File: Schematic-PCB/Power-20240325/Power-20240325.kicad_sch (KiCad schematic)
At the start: 41 parts, among them J1 Conn_01x02_Pin, J2 Conn_01x05_Pin, J3 Conn_01x02_Pin, J4 Conn_01x02_Pin, J5 Conn_01x02_Pin, J6 Conn_01x02_Pin, Q1 PMOS, Q2 NMOS, SW1 SW_SPDT, SW2 Locker-SW, SW3 SW_SPDT, U1 PIC12F683-IMC

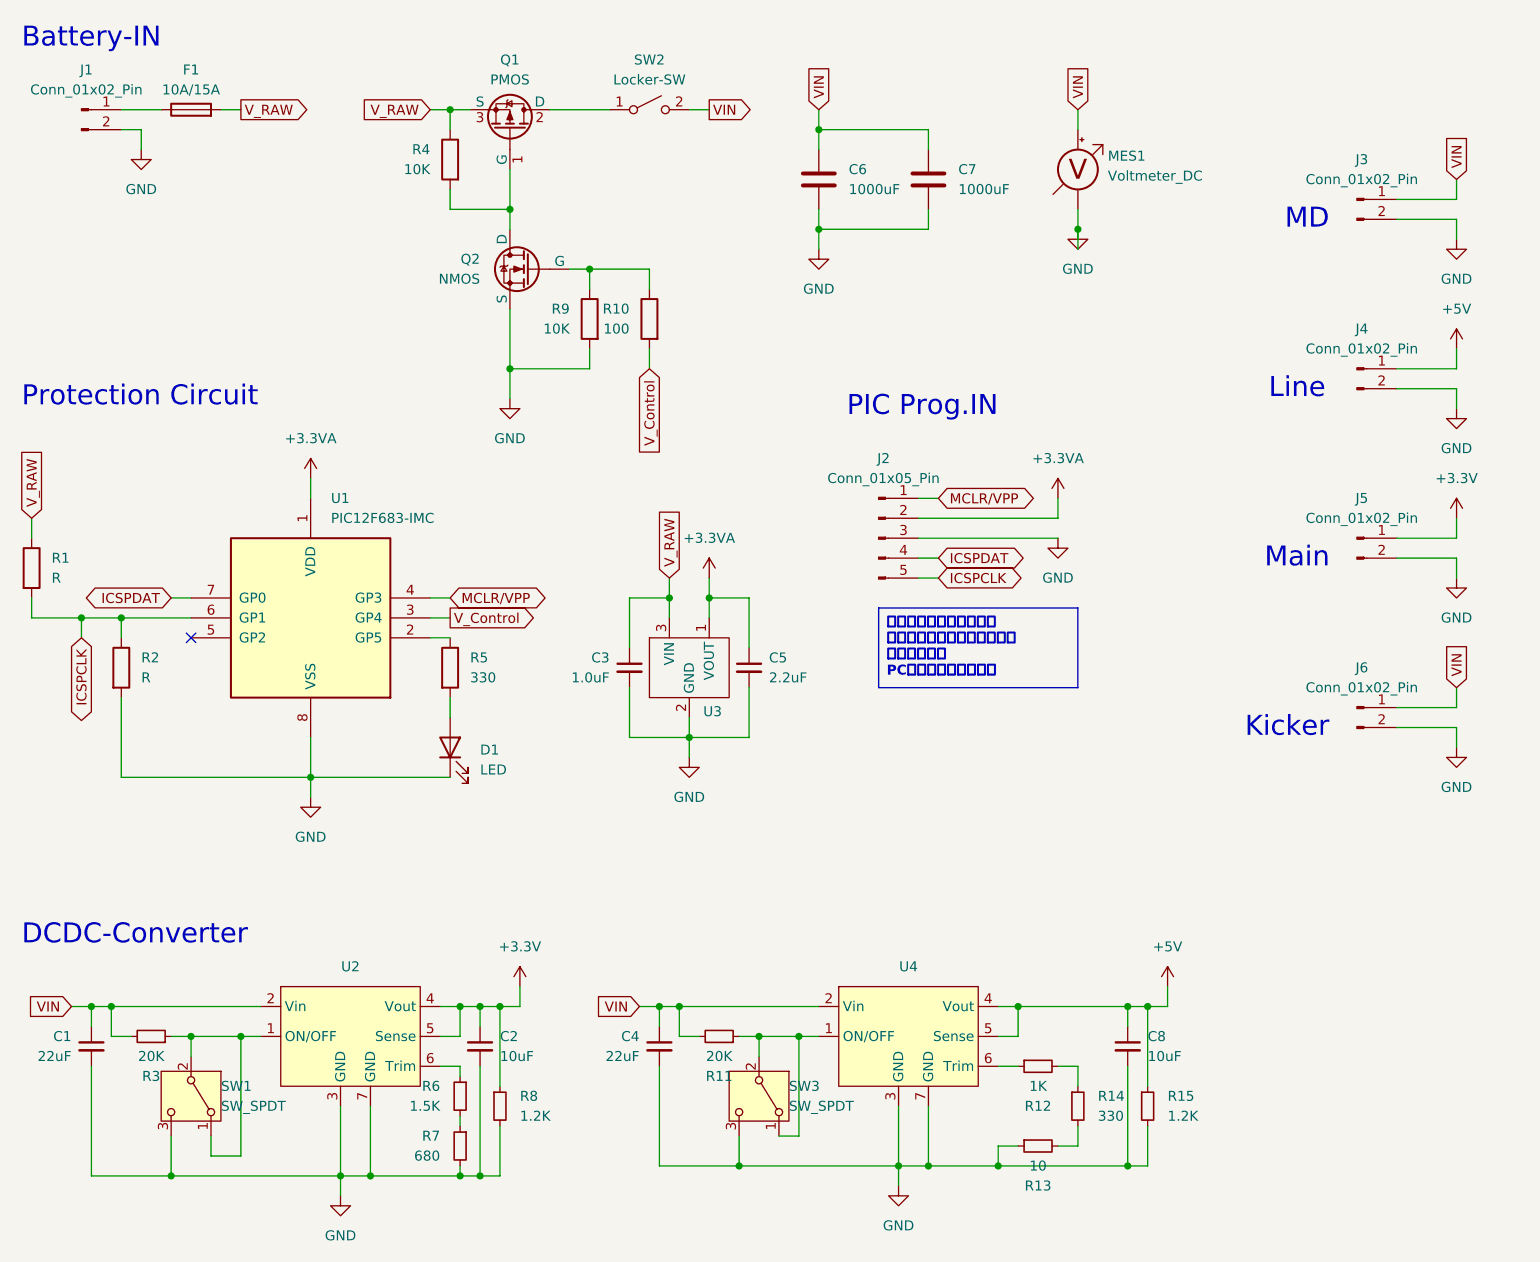
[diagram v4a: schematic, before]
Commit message: 電源基板PCB仮完成
DRをお願いします。
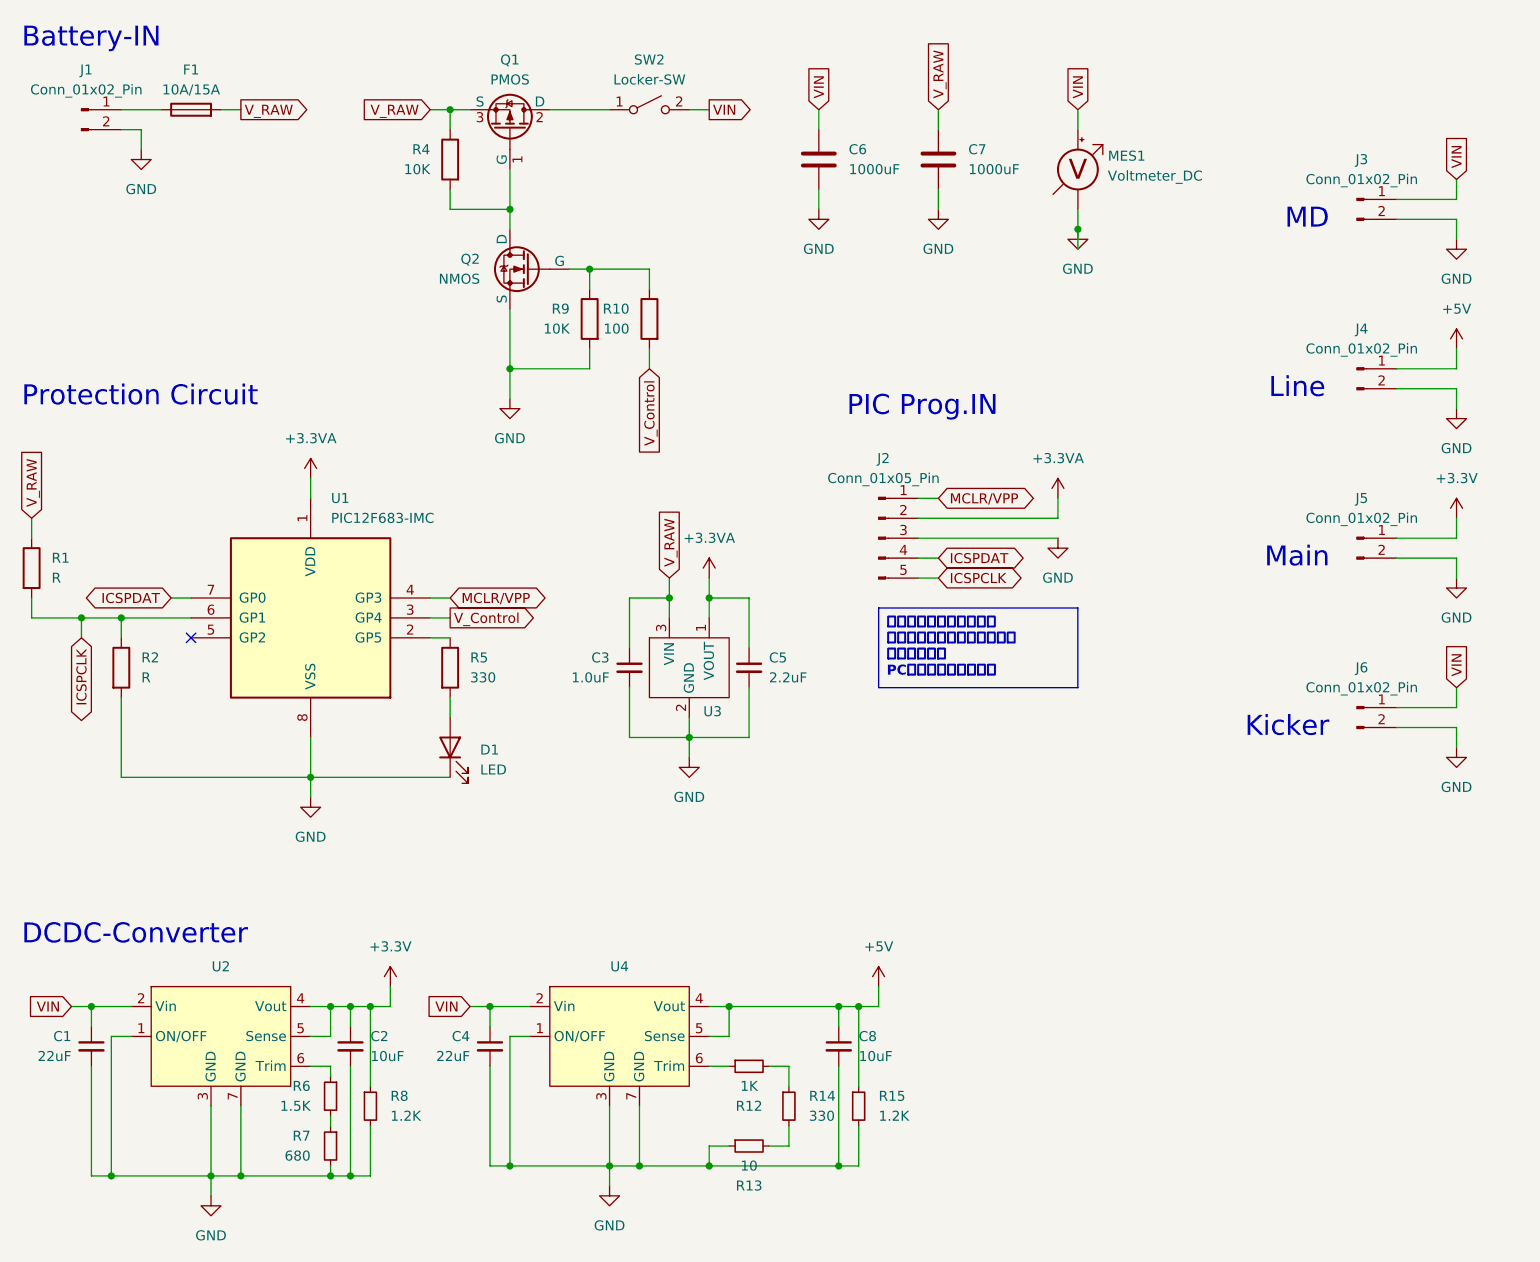
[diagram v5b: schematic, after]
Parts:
- removed R11, R3: 20K, Resistor_SMD:R_0603_1608Metric, symbol Device:R_Small
- removed SW1, SW3: SW_SPDT, @2024-Power:SS12D01G4, symbol Switch:SW_SPDT
- D1: footprint LED_SMD:LED_0805_2012Metric -> LED_THT:LED_D3.0mm
- J3: footprint (none) -> @2024-Power:XT30PW-M
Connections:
- net GND: now also U2.1 (ON/OFF), U4.1 (ON/OFF)
- net VIN: no longer C7.1
- net V_RAW: now also C7.1
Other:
- moved on the sheet: C2, C4, C6, C7, C8, R12, R13, R14, R15, R6, R7, R8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

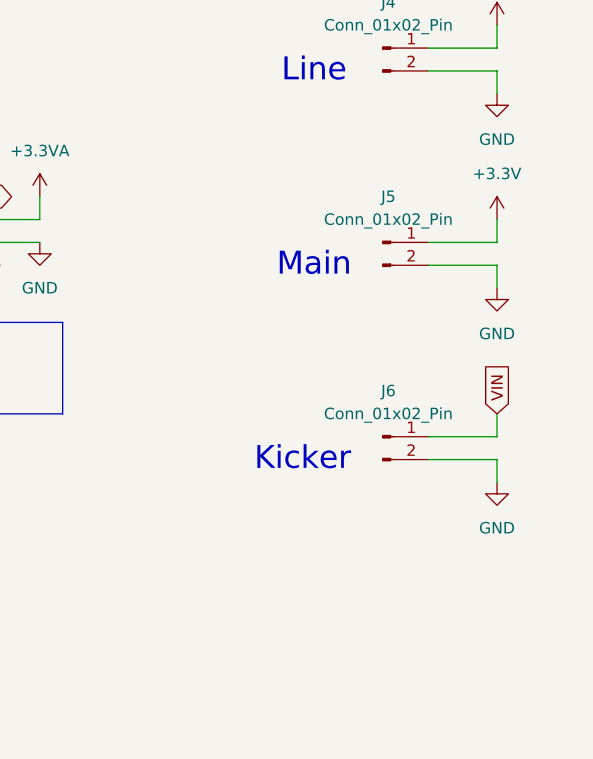
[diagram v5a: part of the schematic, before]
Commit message: 電源基板の回路図/PCBデザインを更新しました。
メイン基板への供給ラインを増やしました。
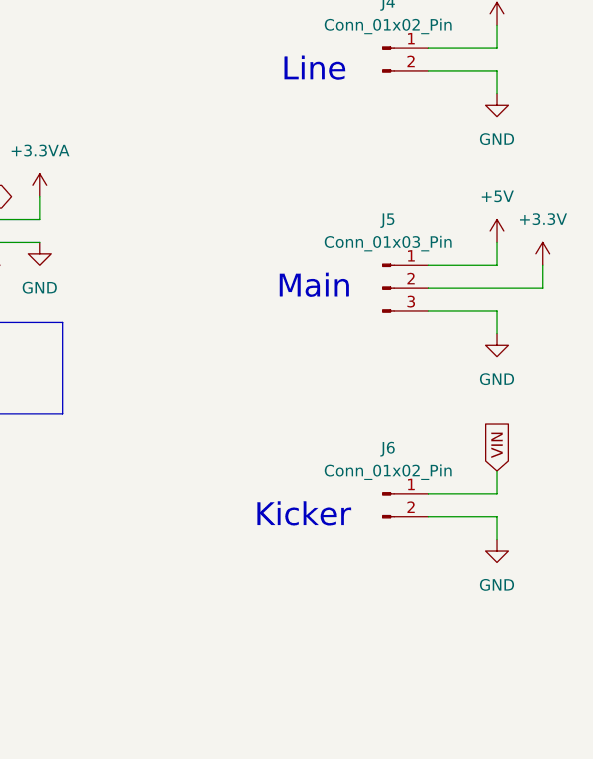
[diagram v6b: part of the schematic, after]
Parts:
- removed J5: Conn_01x02_Pin, Connector_JST:JST_XH_B2B-XH-A_1x02_P2.50mm_Vertical, symbol Connector:Conn_01x02_Pin
- added J5: Conn_01x03_Pin, Connector_JST:JST_XH_B3B-XH-A_1x03_P2.50mm_Vertical, symbol Connector:Conn_01x03_Pin
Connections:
- net +3.3V: now also J5.2 (Pin_2)
- net +5V: now also J5.1 (Pin_1)
- net GND: now also J5.3 (Pin_3)
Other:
- moved on the sheet: J6

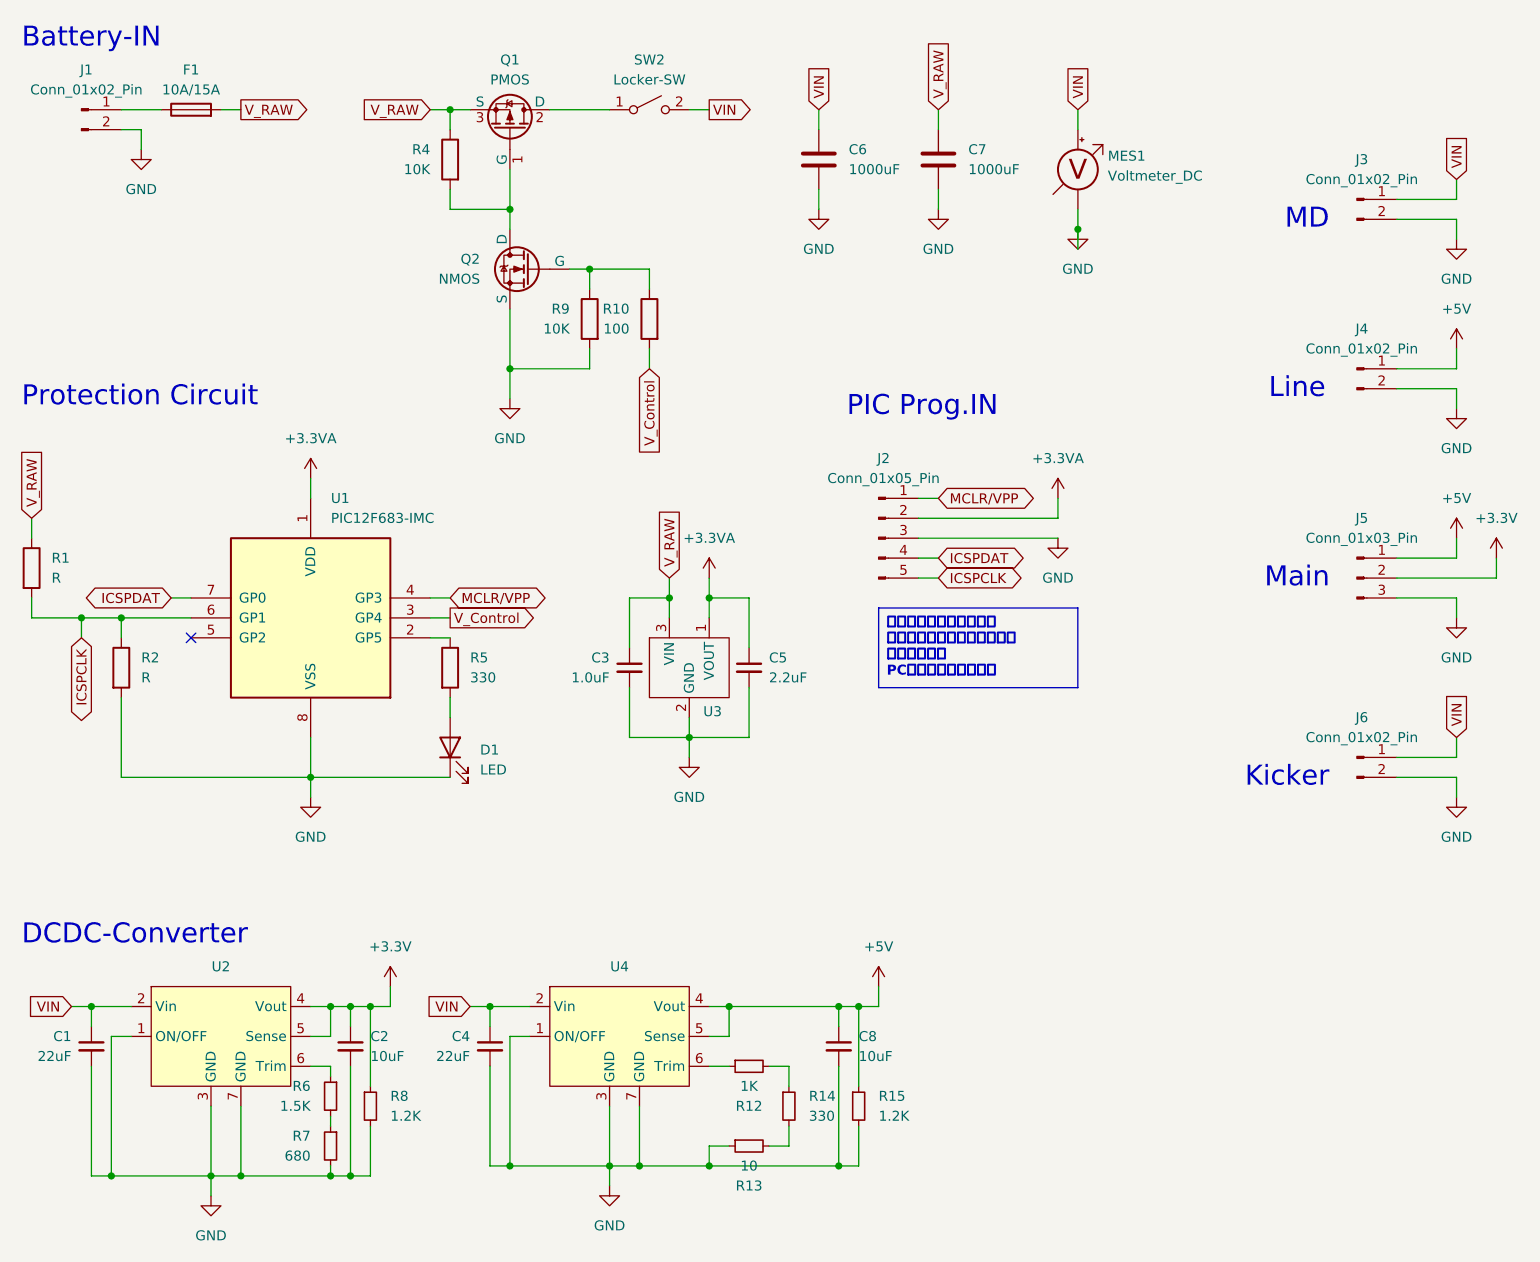
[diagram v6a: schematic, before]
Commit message: キッカーの回路図を更新
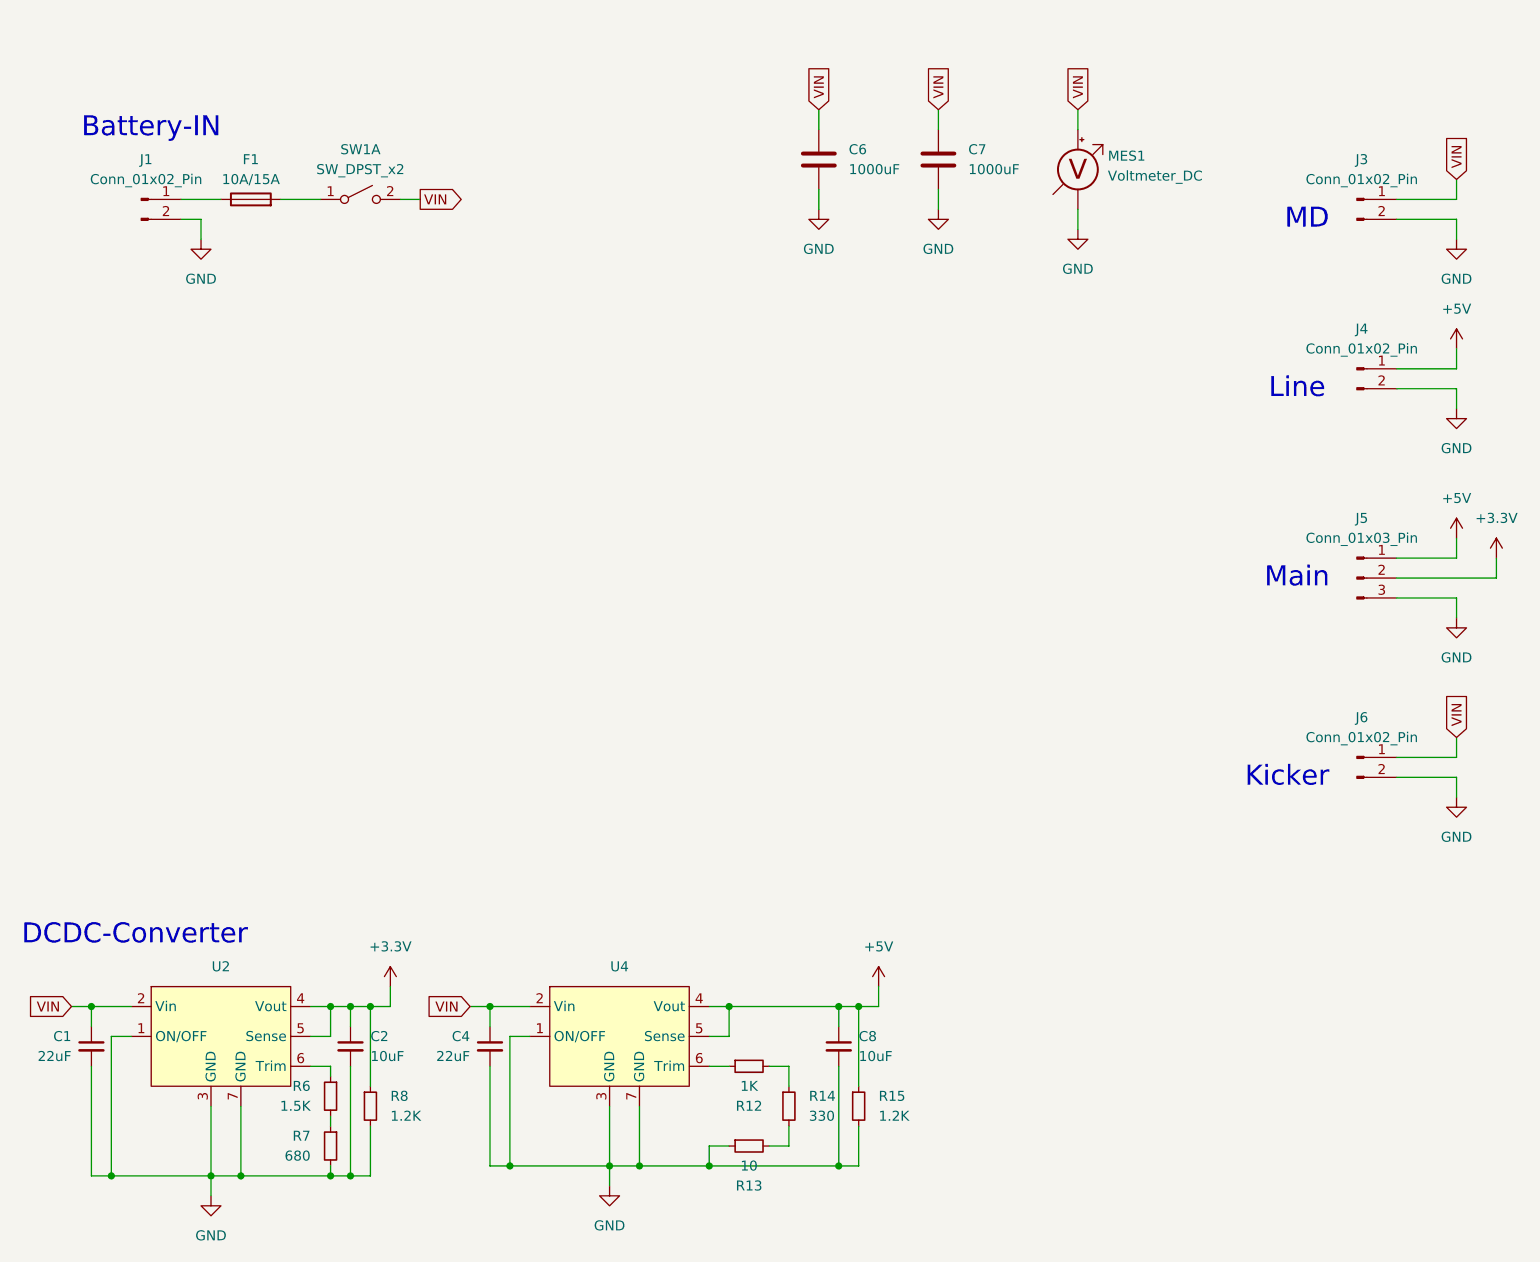
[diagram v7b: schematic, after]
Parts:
- removed C3: 1.0uF, Capacitor_SMD:C_0603_1608Metric, symbol Device:C_Small
- removed C5: 2.2uF, Capacitor_SMD:C_0603_1608Metric, symbol Device:C_Small
- removed D1: LED, LED_THT:LED_D3.0mm, symbol Device:LED
- removed J2: Conn_01x05_Pin, Connector_PinSocket_2.54mm:PinSocket_1x05_P2.54mm_Vertical, symbol Connector:Conn_01x05_Pin
- removed Q1: PMOS, Package_TO_SOT_SMD:TO-252-2, symbol Simulation_SPICE:PMOS
- removed Q2: NMOS, Package_TO_SOT_SMD:SOT-23, symbol @2023_KickerAdjust:NMOS
- removed R1, R2: R, Resistor_THT:R_Axial_DIN0207_L6.3mm_D2.5mm_P7.62mm_Horizontal, symbol Device:R
- removed R10: 100, Resistor_SMD:R_0603_1608Metric, symbol Device:R
- removed R4, R9: 10K, Resistor_SMD:R_0603_1608Metric, symbol Device:R
- removed R5: 330, Resistor_SMD:R_0603_1608Metric, symbol Device:R
- removed SW2: Locker-SW, @2024-Power:RA1113112R, symbol Switch:SW_SPST
- removed U1: PIC12F683-IMC, Package_SO:SOP-8_3.76x4.96mm_P1.27mm, symbol MCU_Microchip_PIC12:PIC12F683-IMC
- removed U3: ~, Package_TO_SOT_SMD:SOT-89-3, symbol @2024-Power:NJW4183U3
- added SW1: SW_DPST_x2, symbol Switch:SW_DPST_x2
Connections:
- net VIN: now also C7.1, SW1.2 (B)
- net V_RAW: no longer names the net of F1.2
- net V_RAW: now also SW1.1 (A); no longer C7.1
- no-connect marks 1 -> 0
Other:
- note removed: "PIC Prog.IN"
- note removed: "Protection Circuit"
- moved on the sheet: F1, J1
